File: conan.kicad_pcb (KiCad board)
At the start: 2 copper layers, 310 parts, among them J1 JST-XH, J10 JST-XH, J11 JST-XH, J12 JST-XH, J13 JST-XH, J14 JST-XH, J15 JST-XH, J16 Stepper, J17 Stepper, J18 Stepper, J19 Stepper, J2 JST-XH, J20 Stepper, J21 Stepper, J22 Boot, J23 UART1, J24 UART2, J25 USB_B_Micro, J26 Endstop 1, J27 Endstop 2, J28 Endstop 1, J29 Endstop 1, J3 JTAG, J30 Endstop 1, J31 Endstop 1, J32 Endstop 1, J33 Endstop 1, J34 Conn_01x02_Male, J35 Thermistor 1, J36 Thermistor 2, J37 Thermistor 3, J38 Thermistor 4, J39 Thermistor 5, J4 JST-XH, J40 Thermistor 6, J41 Thermistor 7, J42 Thermistor 8, J43 pmod, J44 esp8266, J45 Chain_in, J46 Chain_out, J47 Exp1, J48 Display, J49 Exp2, J5 JST-XH, J50 Vaux in, J51 VM2 in, J52 VM1 in, J53 Vaux in, J6 XT60, J7 JST-XH, J8 XT60, J9 JST-XH, Q1 AON7524, Q2 TPH1R405PL, Q3 TPH1R405PL, Q4 AON7524, Q5 AON7524, Q6 AON7524, Q7 AON7524, Q8 AON7524, Q9 Q_NMOS_DGS, SW1 Reset, U1 ECP5U12_CABGA256, U10 TMC2209, U11 TMC2209, U12 TMC2209, U13 TMC2209, U14 AT25xxx, U15 STM32F070CBTx, U16 74VLX244, U17 STWD100, U2 L7986, U3 TLV62569, U4 TLV62569, U5 LP5907MFX-2.5, U6 LP5907MFX-3.3, U7 MIC4127, U8 TMC2209, U9 TMC2209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

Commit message: Recovery after crash, replace double row pin header for expansion by 2 separate single row headers
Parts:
- added J54: Exp2_L, Connector_PinHeader_2.54mm:PinHeader_1x12_P2.54mm_Vertical, F.Cu at (163.0, 33.0)
- added J55: Exp2_R, Connector_PinHeader_2.54mm:PinHeader_1x12_P2.54mm_Vertical, F.Cu at (167.6, 33.0)
- J47: value Exp1 -> Exp2_L; footprint Connector_PinHeader_2.54mm:PinHeader_2x12_P2.54mm_Vertical -> Connector_PinHeader_2.54mm:PinHeader_1x12_P2.54mm_Vertical
- J49: value Exp2 -> Exp2_R; footprint Connector_PinHeader_2.54mm:PinHeader_2x12_P2.54mm_Vertical -> Connector_PinHeader_2.54mm:PinHeader_1x12_P2.54mm_Vertical
- moved J45 124.2 mm to (35.6, 74.9)
- moved J43 104.6 mm to (162.6, 134.6), turned to 270 degrees
- moved R88 104.2 mm to (179.2, 137.3)
- moved R91 104.2 mm to (174.8, 137.3)
- moved R84 104.2 mm to (174.8, 140.2)
- moved R85 104.2 mm to (183.7, 134.3)
- moved R92 104.2 mm to (179.2, 134.3)
- moved R93 104.2 mm to (174.8, 134.3)
- moved J46 101.2 mm to (254.0, 77.5)
- moved R90 87.2 mm to (137.2, 134.3)
- moved R87 87.2 mm to (137.2, 137.3)
- moved R89 87.2 mm to (141.7, 131.4)
- moved R95 87.2 mm to (137.2, 131.4)
- moved J49 31.8 mm to (158.3, 33.0)
- moved J47 20.0 mm to (153.7, 33.0)
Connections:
- J49 pad 1: +Vaux -> +5V
- J49 pad 10: exp2_7 -> exp1_10
- J49 pad 11: exp2_8 -> exp1_9
- J49 pad 3: +3V3 -> exp1_17
- J49 pad 4: exp2_1 -> exp1_16
- J49 pad 5: exp2_2 -> exp1_15
- J49 pad 6: exp2_3 -> exp1_14
- J49 pad 7: exp2_4 -> exp1_13
- J49 pad 8: exp2_5 -> exp1_12
- J49 pad 9: exp2_6 -> exp1_11

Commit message: rough placement
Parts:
- J10: value JST-XH -> PWM11; footprint Connector_JST:JST_XH_B03B-XH-A_1x03_P2.50mm_Vertical -> Connector_JST:JST_PH_B3B-PH-K_1x03_P2.00mm_Vertical
- J11: value JST-XH -> PWM3
- J12: value JST-XH -> PWM7
- J13: value JST-XH -> PWM12; footprint Connector_JST:JST_XH_B03B-XH-A_1x03_P2.50mm_Vertical -> Connector_JST:JST_PH_B3B-PH-K_1x03_P2.00mm_Vertical
- J14: value JST-XH -> PWM4
- J15: value JST-XH -> PWM8
- J26, J27: footprint Connector_JST:JST_XH_B03B-XH-A_1x03_P2.50mm_Vertical -> Connector_JST:JST_PH_B3B-PH-K_1x03_P2.00mm_Vertical
- J28: value Endstop 1 -> Endstop 3; footprint Connector_JST:JST_XH_B03B-XH-A_1x03_P2.50mm_Vertical -> Connector_JST:JST_PH_B3B-PH-K_1x03_P2.00mm_Vertical
- J29: value Endstop 1 -> Endstop 4; footprint Connector_JST:JST_XH_B03B-XH-A_1x03_P2.50mm_Vertical -> Connector_JST:JST_PH_B3B-PH-K_1x03_P2.00mm_Vertical
- J30: value Endstop 1 -> Endstop 5; footprint Connector_JST:JST_XH_B03B-XH-A_1x03_P2.50mm_Vertical -> Connector_JST:JST_PH_B3B-PH-K_1x03_P2.00mm_Vertical
- J31: value Endstop 1 -> Endstop 6; footprint Connector_JST:JST_XH_B03B-XH-A_1x03_P2.50mm_Vertical -> Connector_JST:JST_PH_B3B-PH-K_1x03_P2.00mm_Vertical
- J32: value Endstop 1 -> Endstop 7; footprint Connector_JST:JST_XH_B03B-XH-A_1x03_P2.50mm_Vertical -> Connector_JST:JST_PH_B3B-PH-K_1x03_P2.00mm_Vertical
- J33: value Endstop 1 -> Endstop 8; footprint Connector_JST:JST_XH_B03B-XH-A_1x03_P2.50mm_Vertical -> Connector_JST:JST_PH_B3B-PH-K_1x03_P2.00mm_Vertical
- J34: value Conn_01x02_Male -> Watchdog
- J35, J36, J37, J38, J39, J40, J41, J42: footprint Connector_JST:JST_XH_B02B-XH-A_1x02_P2.50mm_Vertical -> Connector_JST:JST_PH_B2B-PH-K_1x02_P2.00mm_Vertical
- J4: value JST-XH -> PWM9; footprint Connector_JST:JST_XH_B03B-XH-A_1x03_P2.50mm_Vertical -> Connector_JST:JST_PH_B3B-PH-K_1x03_P2.00mm_Vertical
- J47: value Exp2_L -> Exp1_L
- J49: value Exp2_R -> Exp1_R
- J5: value JST-XH -> PWM5
- J6: value XT60 -> PWM1_HP
- J7: value JST-XH -> PWM10; footprint Connector_JST:JST_XH_B03B-XH-A_1x03_P2.50mm_Vertical -> Connector_JST:JST_PH_B3B-PH-K_1x03_P2.00mm_Vertical
- J8: value XT60 -> PWM2_HP
- J9: value JST-XH -> PWM6
- JP11: value Jumper_3_Bridged12 -> Endstop_1-6_select
- JP12: value Jumper_3_Bridged12 -> Endstop_7-8_select
- JP2: value Jumper_3_Bridged12 -> PWM_9-10_select
- JP3: value Jumper_3_Bridged12 -> PWM_5-8_select
- JP4: value Jumper_3_Bridged12 -> PWM_12-13_select
- moved C92 224.8 mm to (21.4, 115.8)
- moved C97 220.0 mm to (21.4, 113.8)
- moved C96 216.6 mm to (21.4, 117.9)
- moved C91 215.5 mm to (25.5, 114.3)
- moved C93 215.2 mm to (21.4, 120.4)
- moved C94 215.2 mm to (21.3, 111.8)
- moved C95 213.7 mm to (21.4, 122.4)
- moved J22 196.1 mm to (36.6, 109.2), turned to 90 degrees
- moved C90 195.1 mm to (25.5, 111.8)
- moved R51 193.7 mm to (47.3, 106.2)
- moved R50 193.6 mm to (38.7, 105.7)
- moved C87 191.6 mm to (39.0, 103.1)
- moved J23 191.5 mm to (43.9, 123.2), turned to 90 degrees
- moved R55 187.8 mm to (60.3, 114.6)
- moved R53 178.9 mm to (71.1, 120.3), turned to 90 degrees
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
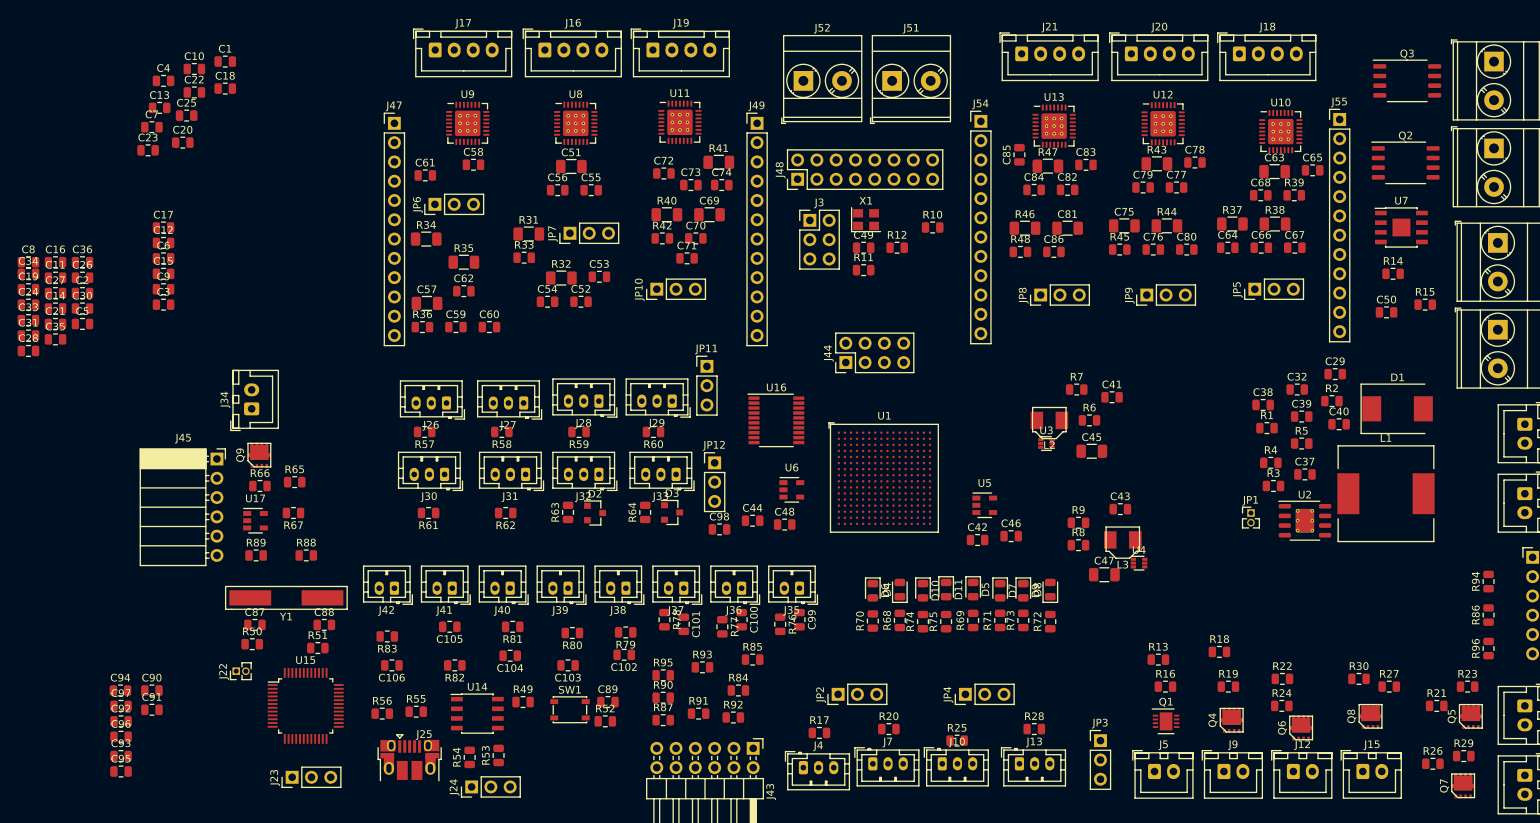
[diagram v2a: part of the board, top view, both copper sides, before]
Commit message: better footprints for restistors and capacitors
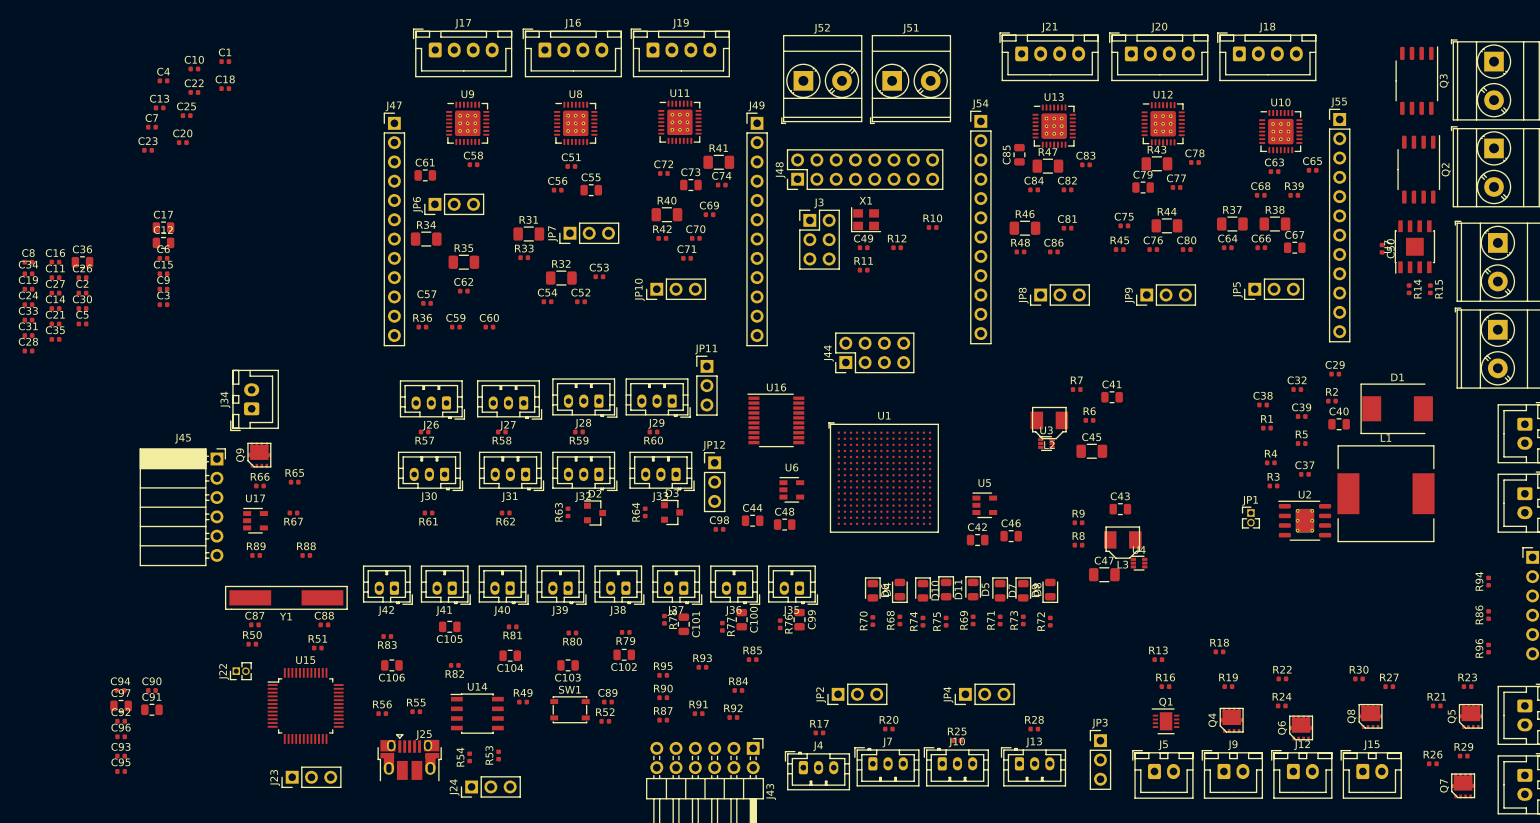
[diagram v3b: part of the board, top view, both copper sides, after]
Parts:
- C1, C10, C11, C13, C14, C15, C16, C18, C19, C2, C20, C21, C22, C23, C24, C25, C26, C27, C28, C29, C3, C30, C31, C32, C33, C34, C35, C37, C38, C39, C4, C49, C5, C50, C52, C53, C54, C56, C58, C59, C6, C60, C62, C64, C65, C66, C68, C7, C70, C71, C72, C74, C76, C77, C78, C8, C80, C82, C83, C84, C86, C87, C88, C89, C9, C90, C92, C93, C94, C95, C96, C98: footprint Capacitor_SMD:C_0805_2012Metric -> Capacitor_SMD:C_0402_1005Metric
- C51, C57, C63, C69, C75, C81: footprint Capacitor_SMD:C_1206_3216Metric -> Capacitor_SMD:C_0402_1005Metric
- R1, R10, R11, R12, R13, R14, R15, R16, R17, R18, R19, R2, R20, R21, R22, R23, R24, R25, R26, R27, R28, R29, R3, R30, R33, R36, R39, R4, R42, R45, R48, R49, R5, R50, R51, R52, R53, R54, R55, R56, R57, R58, R59, R6, R60, R61, R62, R63, R64, R65, R66, R67, R68, R69, R7, R70, R71, R72, R73, R74, R75, R76, R77, R78, R79, R8, R80, R81, R82, R83, R84, R85, R86, R87, R88, R89, R9, R90, R91, R92, R93, R94, R95, R96: footprint Resistor_SMD:R_0805_2012Metric -> Resistor_SMD:R_0402_1005Metric
- moved C50 8.40 mm to (187.5, 53.6), turned to 270 degrees
- moved U7 3.10 mm to (191.8, 53.3), turned to 90 degrees
- moved R14 2.93 mm to (191.0, 58.9), turned to 270 degrees
- moved R15 2.14 mm to (193.8, 58.9), turned to 270 degrees
- moved Q2 1.94 mm to (192.3, 43.2), turned to 270 degrees
- moved Q3 1.27 mm to (192.0, 31.5), turned to 270 degrees

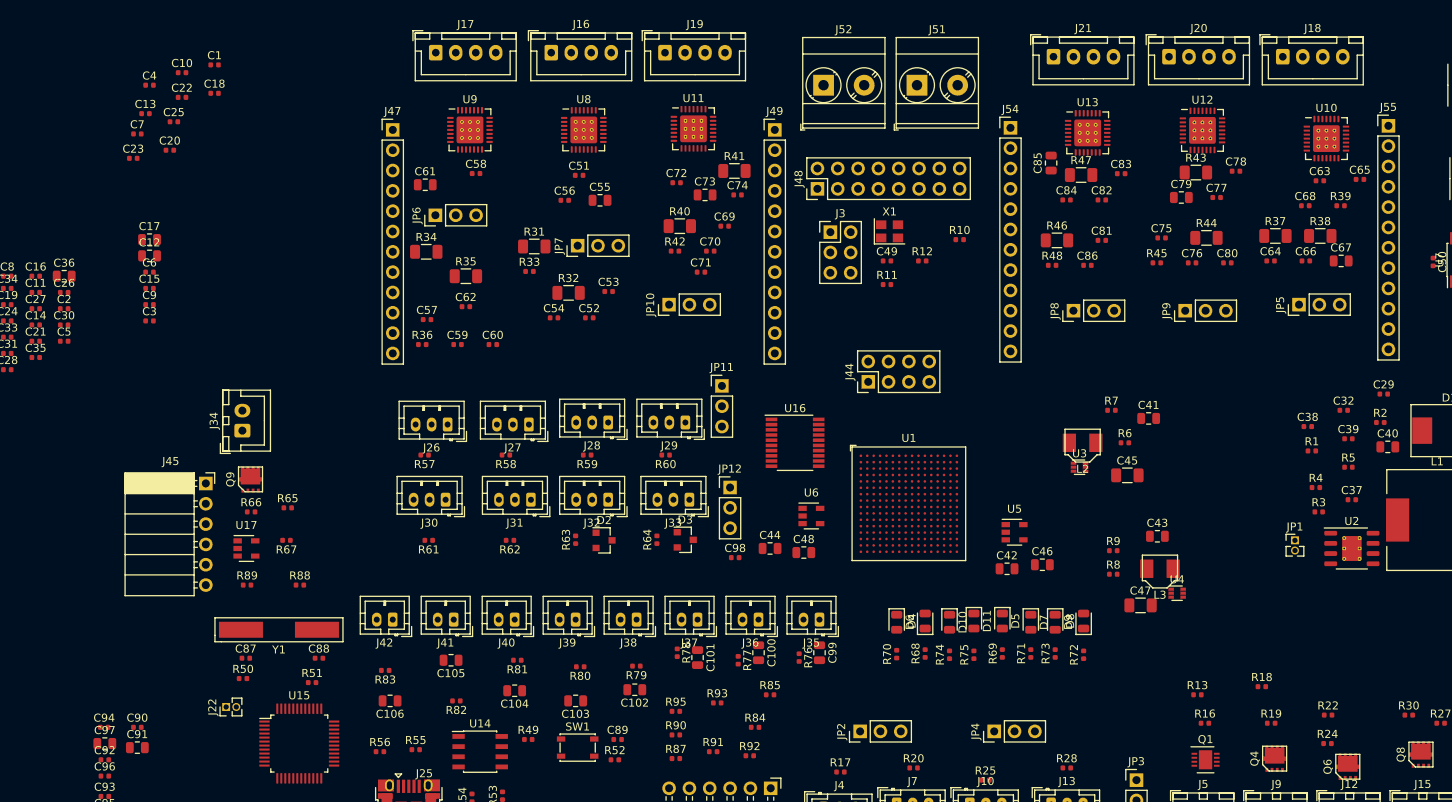
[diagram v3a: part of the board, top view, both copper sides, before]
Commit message: More footprint updates, removed individual ENN pullups for drivers
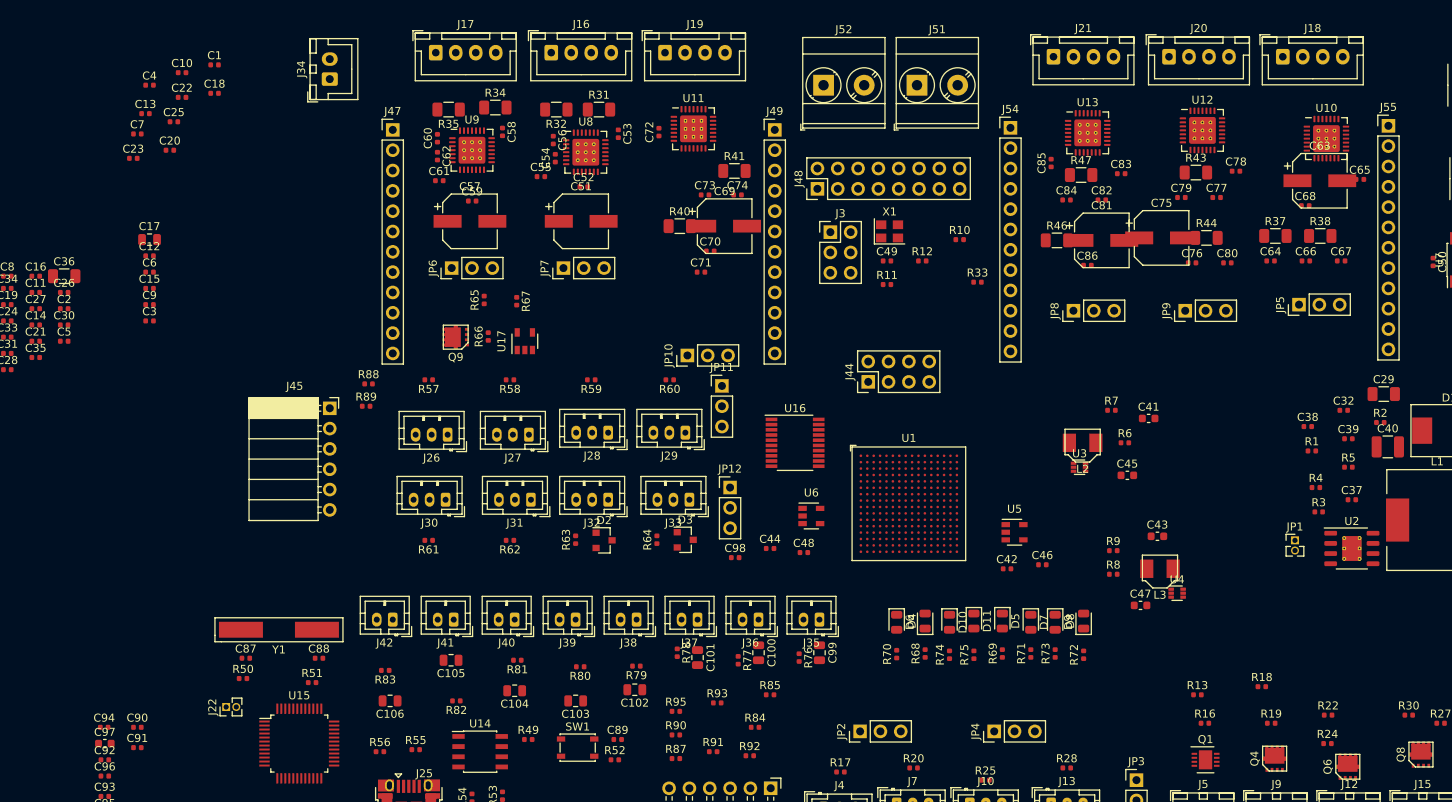
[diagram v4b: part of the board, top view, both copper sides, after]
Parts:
- removed R36, R39, R42, R45, R48: 10k, Resistor_SMD:R_0402_1005Metric
- C12, C42, C44, C46, C48, C55, C61, C67, C73, C79, C85, C91: footprint Capacitor_SMD:C_0805_2012Metric -> Capacitor_SMD:C_0402_1005Metric
- C29: value 10uF -> 10uF/ceramic/50V/8mOhm; footprint Capacitor_SMD:C_0402_1005Metric -> Capacitor_SMD:C_1206_3216Metric
- C32: value 220nF -> 220nF/50V
- C36: footprint Capacitor_SMD:C_0805_2012Metric -> Capacitor_SMD:C_1206_3216Metric
- C40: value 68uF -> 68uF/tantalum/6.3V/100mOhm; footprint Capacitor_SMD:C_0805_2012Metric -> Capacitor_SMD:C_1210_3225Metric
- C41, C43: value 4.7uF -> 4.7uF/10V/ceramic/0603; footprint Capacitor_SMD:C_0805_2012Metric -> Capacitor_SMD:C_0603_1608Metric
- C45, C47: value 22uF -> 22uF/6.3V/4mOhm/ceramic; footprint Capacitor_SMD:C_1206_3216Metric -> Capacitor_SMD:C_0603_1608Metric
- C51, C57, C63, C69, C75, C81: value 100u -> 100uF/50V/lowESR; footprint Capacitor_SMD:C_0402_1005Metric -> Capacitor_SMD:CP_Elec_6.3x5.9
- C52, C53, C58, C59, C64, C65, C70, C71, C76, C77, C82, C83: value 100n -> 100nF/50V
- C54, C60, C66, C72, C78, C84: value 100n -> 100n/16V
- C56, C62, C68, C74, C80, C86: value 100n/50V -> 22n/50V
- C97: footprint Capacitor_SMD:C_0805_2012Metric -> Capacitor_SMD:C_0603_1608Metric
- moved R33 56.0 mm to (130.5, 56.1)
- moved J34 45.3 mm to (49.5, 30.7)
- moved U17 43.4 mm to (73.9, 63.5), turned to 90 degrees
- moved R67 41.5 mm to (72.9, 58.5), turned to 270 degrees
- moved R66 36.9 mm to (69.3, 62.9), turned to 90 degrees
- moved R65 35.8 mm to (68.8, 58.3), turned to 90 degrees
- moved Q9 31.2 mm to (65.3, 63.0), turned to 90 degrees
- moved R89 26.9 mm to (54.1, 71.6)
- moved C60 26.7 mm to (63.0, 38.1), turned to 90 degrees
- moved R88 26.6 mm to (54.4, 68.8)
- moved R32 23.0 mm to (77.8, 34.5), turned to 180 degrees
- moved R35 20.9 mm to (64.4, 34.5), turned to 180 degrees
- moved R34 20.0 mm to (70.2, 34.3)
- moved C54 20.0 mm to (77.7, 40.6), turned to 90 degrees
- moved C53 19.8 mm to (85.6, 37.6), turned to 270 degrees
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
